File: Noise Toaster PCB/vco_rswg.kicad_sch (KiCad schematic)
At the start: 21 parts, among them Q1 NJFET, U1 LM324, U2 LM324

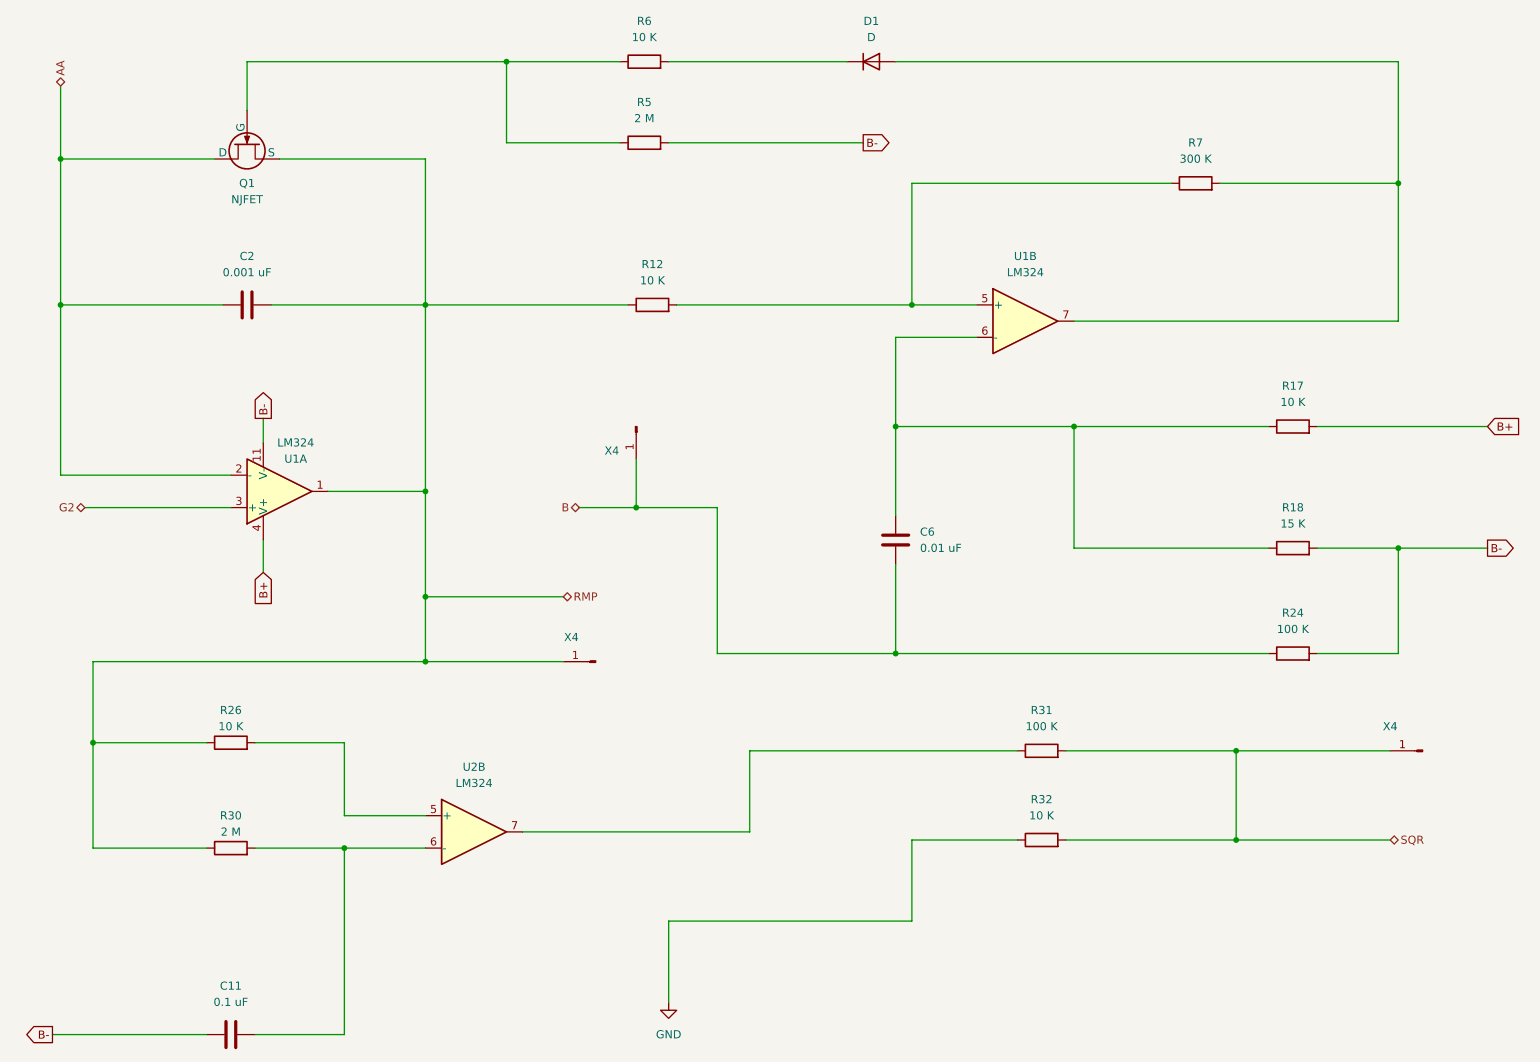
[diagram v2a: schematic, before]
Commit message: refactored schematics and added front panel
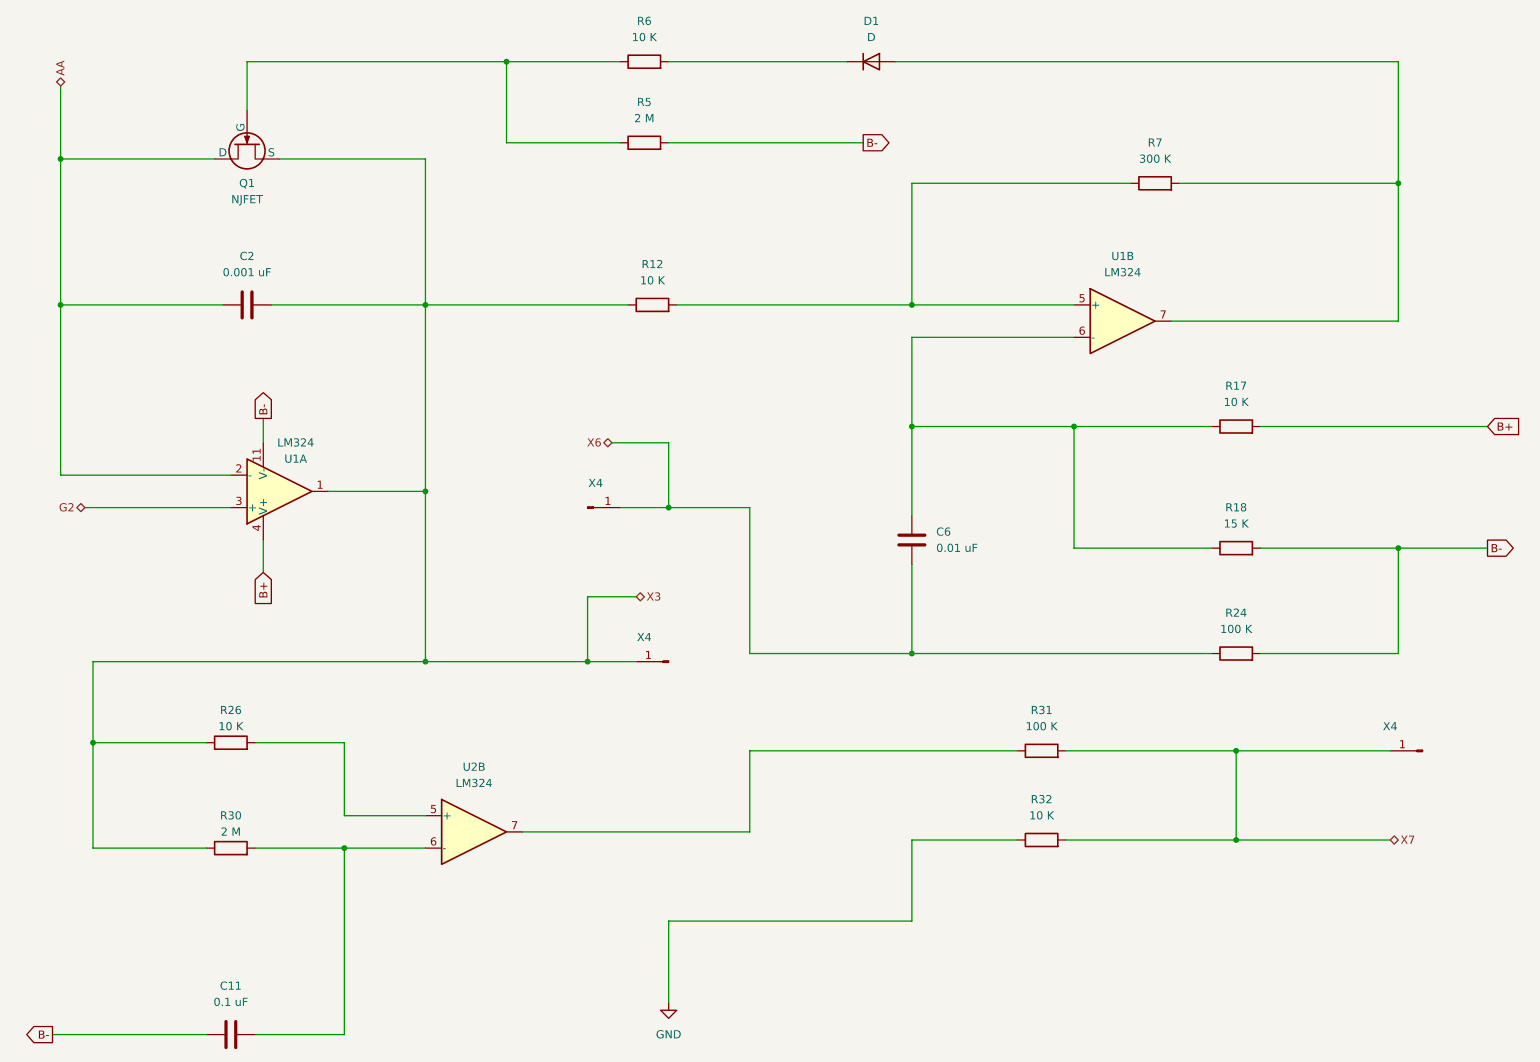
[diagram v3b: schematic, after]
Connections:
- net B renamed X6
- net RMP renamed X3
- net SQR renamed X7
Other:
- moved on the sheet: C6, R17, R18, R24, R7, U1B, X4

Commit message: wireing and components have been checked
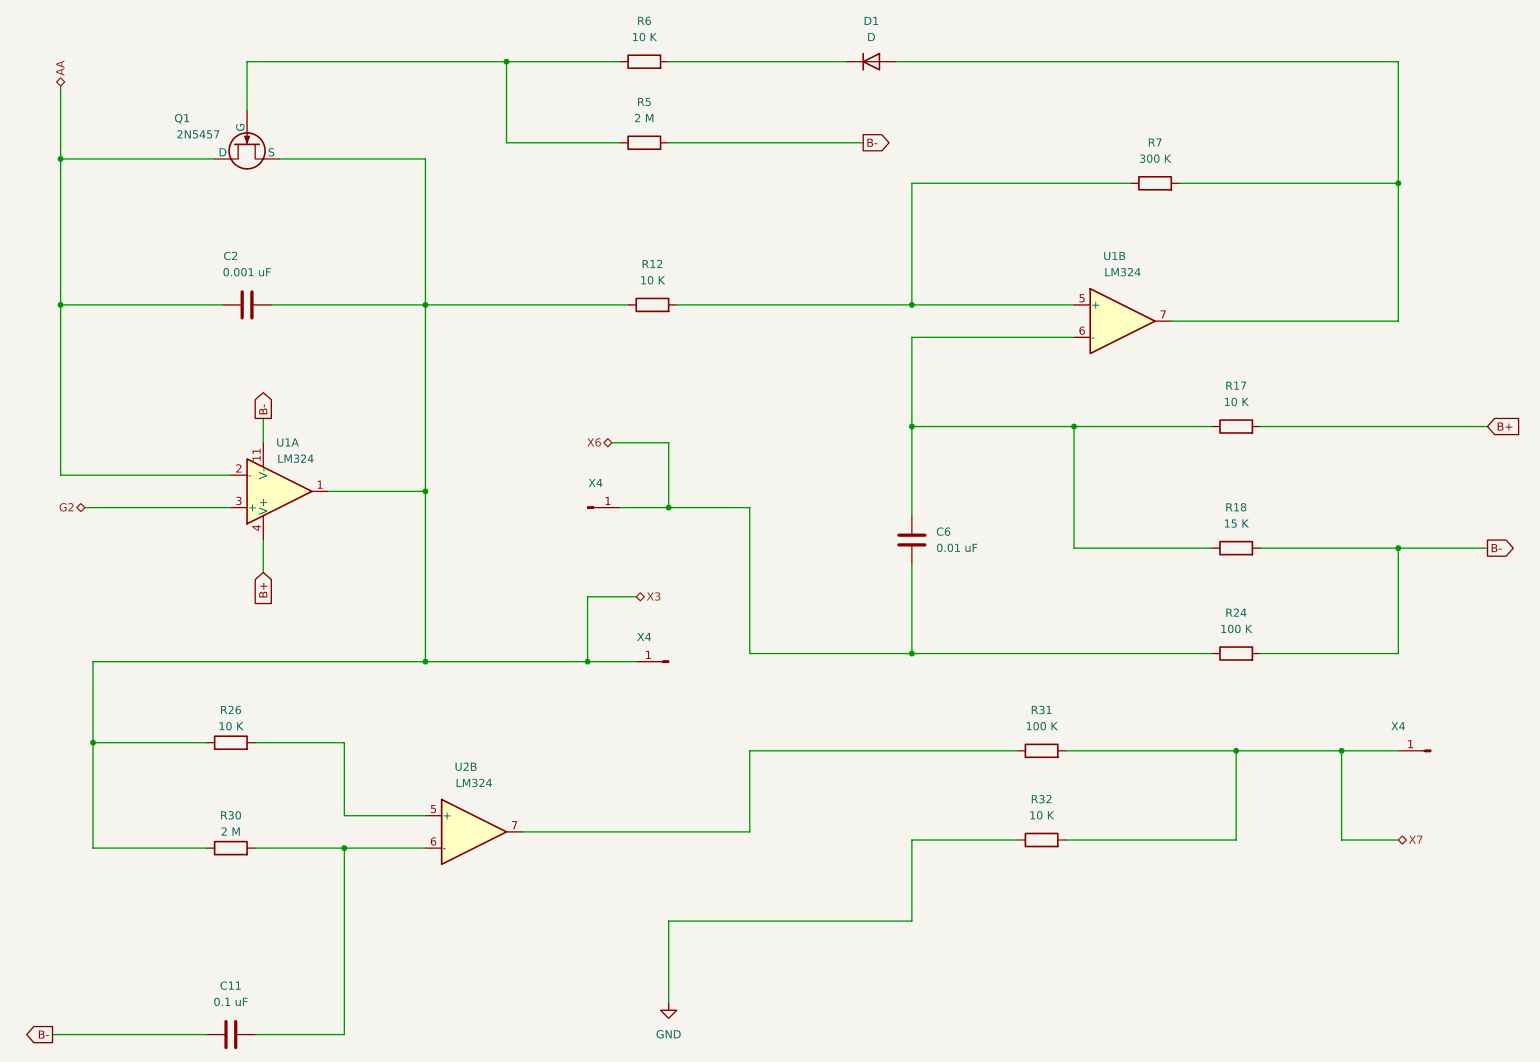
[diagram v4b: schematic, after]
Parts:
- Q1: value NJFET -> 2N5457
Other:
- moved on the sheet: X4
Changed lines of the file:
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@@
   (junction (at 88.9 92.71) (diameter 0) (color 0 0 0 0)
   )
-  (junction (at 215.9 147.32) (diameter 0) (color 0 0 0 0)
-  )
   (junction (at 36.83 132.08) (diameter 0) (color 0 0 0 0)
   )
   (junction (at 241.3 44.45) (diameter 0) (color 0 0 0 0)
   )
+  (junction (at 232.41 133.35) (diameter 0) (color 0 0 0 0)
+  )
   (junction (at 127 95.25) (diameter 0) (color 0 0 0 0)
   )
@@
   (junction (at 88.9 63.5) (diameter 0) (color 0 0 0 0)
   )
+  (wire (pts (xy 232.41 147.32) (xy 232.41 133.35))
+    (stroke (width 0) (type default))
+  )
   (wire (pts (xy 127 95.25) (xy 139.7 95.25))
     (stroke (width 0) (type default))
@@
     (stroke (width 0) (type default))
   )
-  (wire (pts (xy 215.9 133.35) (xy 240.03 133.35))
+  (wire (pts (xy 215.9 133.35) (xy 232.41 133.35))
     (stroke (width 0) (type default))
   )
@@
     (stroke (width 0) (type default))
   )
-  (wire (pts (xy 215.9 147.32) (xy 240.03 147.32))
-    (stroke (width 0) (type default))
-  )
   (wire (pts (xy 165.1 68.58) (xy 165.1 82.55))
     (stroke (width 0) (type default))
@@
     (stroke (width 0) (type default))
   )
+  (wire (pts (xy 232.41 133.35) (xy 241.3 133.35))
+    (stroke (width 0) (type default))
+  )
   (wire (pts (xy 101.6 25.4) (xy 101.6 38.1))
     (stroke (width 0) (type default))
@@
   )
   (wire (pts (xy 127 25.4) (xy 154.94 25.4))
+    (stroke (width 0) (type default))
+  )
+  (wire (pts (xy 241.3 147.32) (xy 232.41 147.32))
     (stroke (width 0) (type default))
   )
@@
     )
   )
-  (hierarchical_label "X7" (shape bidirectional) (at 240.03 147.32 0)
+  (hierarchical_label "X7" (shape bidirectional) (at 241.3 147.32 0)
     (effects (font (size 1.27 1.27)) (justify left))
-    (property "Bezeichnung" "SQR" (at 242.57 149.86 0)
+    (property "Bezeichnung" "SQR" (at 243.84 149.86 0)
       (effects (font (size 1.27 1.27) italic) (justify left))
     )
   )
   (symbol (lib_id "Amplifier_Operational:LM324") (at 96.52 146.05 0) (unit 2)
-    (in_bom yes) (on_board yes) (dnp no) (fields_autoplaced)
-    (property "Reference" "U2" (at 96.52 135.89 0)
+    (in_bom yes) (on_board yes) (dnp no)
+    (property "Reference" "U2" (at 95.25 135.89 0)
       (effects (font (size 1.27 1.27)))
     )
@@
     )
   )
-  (symbol (lib_id "Connector:Conn_01x01_Pin") (at 245.11 133.35 180) (unit 1)
-    (in_bom yes) (on_board yes) (dnp no)
-    (property "Reference" "X4" (at 240.03 129.54 0)
-      (effects (font (size 1.27 1.27)))
-    )
-    (property "Value" "~" (at 244.475 135.89 0)
-      (effects (font (size 1.27 1.27)))
-    )
-    (property "Footprint" "" (at 245.11 133.35 0)
-      (effects (font (size 1.27 1.27)) hide)
-    )
-    (property "Datasheet" "~" (at 245.11 133.35 0)
+  (symbol (lib_id "Connector:Conn_01x01_Pin") (at 246.38 133.35 180) (unit 1)
+    (in_bom yes) (on_board yes) (dnp no)
+    (property "Reference" "X4" (at 241.3 129.54 0)
+      (effects (font (size 1.27 1.27)))
+    )
+    (property "Value" "~" (at 245.745 135.89 0)
+      (effects (font (size 1.27 1.27)))
+    )
+    (property "Footprint" "" (at 246.38 133.35 0)
+      (effects (font (size 1.27 1.27)) hide)
+    )
+    (property "Datasheet" "~" (at 246.38 133.35 0)
       (effects (font (size 1.27 1.27)) hide)
     )
@@
   )
   (symbol (lib_id "Amplifier_Operational:LM324") (at 198.12 66.04 0) (unit 2)
-    (in_bom yes) (on_board yes) (dnp no) (fields_autoplaced)
-    (property "Reference" "U1" (at 198.12 55.88 0)
+    (in_bom yes) (on_board yes) (dnp no)
+    (property "Reference" "U1" (at 196.85 55.88 0)
       (effects (font (size 1.27 1.27)))
     )
@@
   )
   (symbol (lib_id "Device:C") (at 60.96 63.5 90) (unit 1)
-    (in_bom yes) (on_board yes) (dnp no) (fields_autoplaced)
-    (property "Reference" "C2" (at 60.96 55.88 90)
+    (in_bom yes) (on_board yes) (dnp no)
+    (property "Reference" "C2" (at 58.42 55.88 90)
       (effects (font (size 1.27 1.27)))
     )
@@
   (symbol (lib_id "Amplifier_Operational:LM324") (at 66.04 92.71 0) (mirror x) (unit 1)
     (in_bom yes) (on_board yes) (dnp no)
-    (property "Reference" "U1" (at 68.58 87.63 0)
-      (effects (font (size 1.27 1.27)))
-    )
-    (property "Value" "LM324" (at 68.58 85.09 0)
+    (property "Reference" "U1" (at 67.31 85.09 0)
+      (effects (font (size 1.27 1.27)))
+    )
+    (property "Value" "LM324" (at 68.58 87.63 0)
       (effects (font (size 1.27 1.27)))
     )
@@
   (symbol (lib_id "Simulation_SPICE:NJFET") (at 60.96 38.1 90) (mirror x) (unit 1)
     (in_bom yes) (on_board yes) (dnp no)
-    (property "Reference" "Q1" (at 60.96 44.45 90)
-      (effects (font (size 1.27 1.27)))
-    )
-    (property "Value" "NJFET" (at 60.96 46.99 90)
-      (effects (font (size 1.27 1.27)))
-    )
+    (property "Reference" "Q1" (at 50.8 34.29 90)
+      (effects (font (size 1.27 1.27)))
+    )
+    (property "Value" "2N5457" (at 53.34 36.83 90)
+      (effects (font (size 1.27 1.27)))
+    )
